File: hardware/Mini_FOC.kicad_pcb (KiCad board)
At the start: 4 copper layers, 63.7 x 41.7 mm, 41 parts, among them J1 Conn_01x03_Socket, J2 Conn_01x06_Socket, J3 Conn_01x04_Socket, J4 Conn_01x04_Socket, J5 Conn_01x02_Socket, J6 Conn_01x06_Socket, SW1 SW_SPDT, U1 DRV8313PWPR, U2 STM32F103C8T6, U3 AMS1117-3.3, U4 LM2596SX-5.0/NOPB, Y2 8MHz

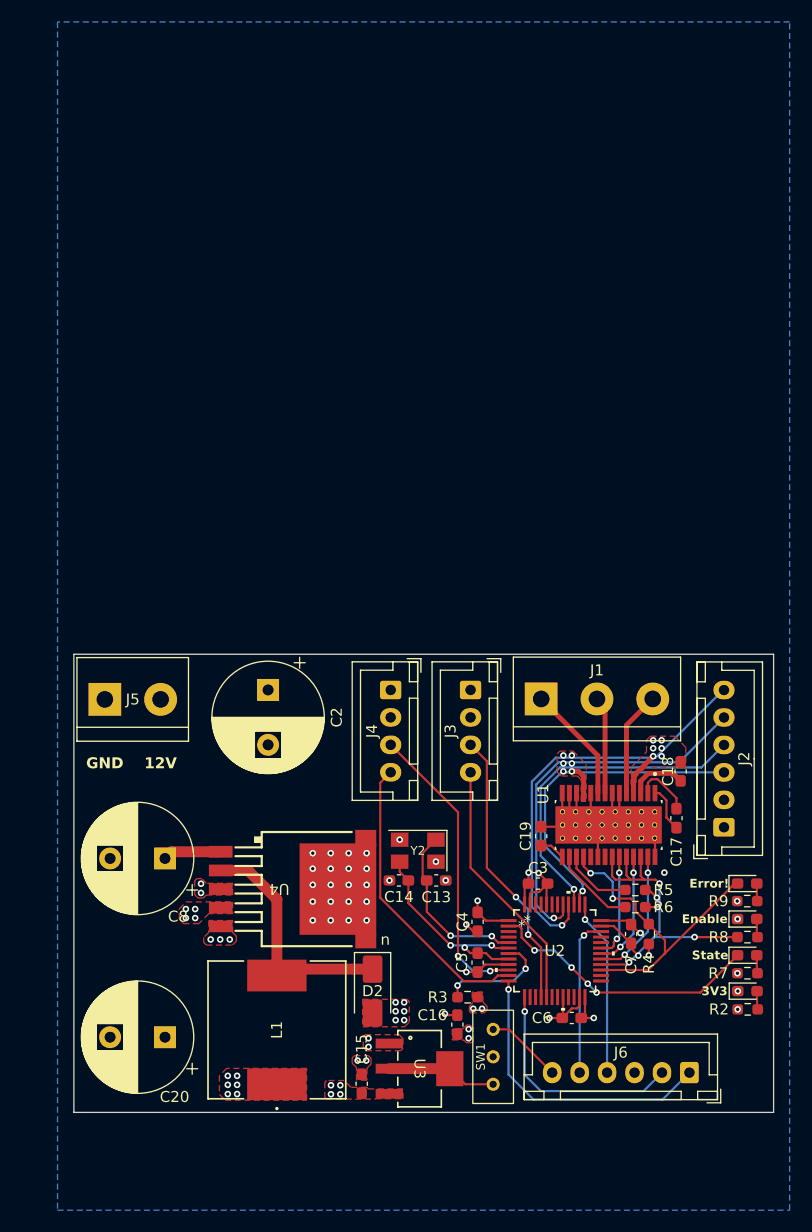
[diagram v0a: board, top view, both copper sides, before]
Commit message: minimize the pcb & add logo
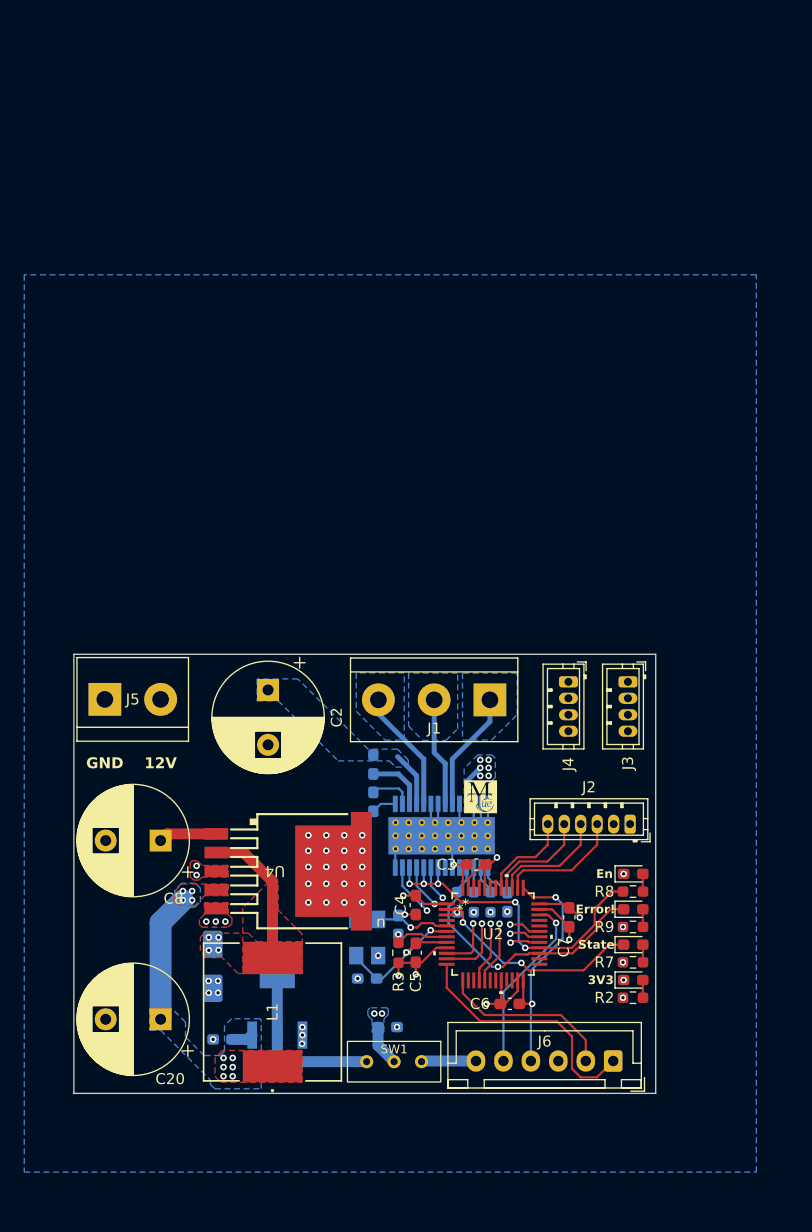
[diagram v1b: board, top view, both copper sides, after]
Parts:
- added G***: LOGO, tue_logo:logo3x3, F.Cu at (85.8, 84.6)
- C13, C14, C15, C16, C17, C18, C19, D2, R4, R5, R6, U1, U3, Y2: moved to B.Cu
- J2: footprint Connector_JST:JST_XH_B6B-XH-A_1x06_P2.50mm_Vertical -> Connector_JST:JST_ZH_B6B-ZR_1x06_P1.50mm_Vertical
- J3, J4: footprint Connector_JST:JST_XH_B4B-XH-A_1x04_P2.50mm_Vertical -> Connector_JST:JST_ZH_B4B-ZR_1x04_P1.50mm_Vertical
- moved C18 28.0 mm to (76.1, 81.7)
- moved C17 27.7 mm to (76.1, 85.1)
- moved R4 17.7 mm to (83.7, 94.2)
- moved J4 16.2 mm to (93.8, 74.1)
- moved U1 15.2 mm to (82.3, 88.2)
- moved R5 14.8 mm to (85.2, 94.2), turned to -90 degrees
- moved D2 14.7 mm to (61.4, 100.0)
- moved J3 14.4 mm to (99.3, 74.1)
- moved U3 14.2 mm to (67.3, 103.6), turned to 180 degrees
- moved C15 13.3 mm to (62.3, 106.7), turned to 180 degrees
- moved R6 13.2 mm to (86.7, 94.2), turned to -90 degrees
- moved R8 11.2 mm to (99.7, 93.2)
- moved D4 11.2 mm to (99.7, 91.6)
- moved R9 10.7 mm to (99.7, 96.5)
- moved D5 10.6 mm to (99.7, 94.8)
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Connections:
- J2 pad 5: SPI_MOSI -> SPI_MISO
- J2 pad 6: SPI_MISO -> SPI_MOSI
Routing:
- net SPI_MISO: track 38.0 -> 9.47 mm, vias 1 -> 0
- net SPI_MOSI: track 34.6 -> 8.51 mm, vias 1 -> 0
- net SPI_CLK: track 30.3 -> 10.4 mm, vias 1 -> 0
- net SPI_SS: track 29.0 -> 11.4 mm, vias 1 -> 0
- net +5V: track 0.08 -> 13.7 mm, vias 14 -> 10
- net Net-(U2A-OSC_IN): track 15.8 -> 7.11 mm, vias 2 -> 1
- net ENC2_CH2: track 23.3 -> 31.8 mm, vias 0 -> 1
- net Net-(D2-K): track 22.1 -> 14.0 mm, vias 0 -> 4
- net ENC2_CH1: track 25.6 -> 32.9 mm, vias 2 -> 1
- net Net-(U2A-NRST): track 10.5 -> 4.82 mm, vias 2 -> 0
- net 3v3_ldo: track 10.0 -> 15.7 mm
- net PWM3: track 9.57 -> 14.9 mm
- net LED_PC13: track 25.3 -> 19.9 mm, vias 4 -> 2
- net PWM2: track 10.7 -> 15.8 mm
- net Net-(U1-~{RESET}): track 7.61 -> 2.60 mm
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- added copper zone on B.Cu, net +12V
- added copper zone on B.Cu, net +3V3
- added copper zone on B.Cu, net +5V
- added copper zone on B.Cu, net MOTOR_PH1
- added copper zone on B.Cu, net MOTOR_PH2
- added copper zone on B.Cu, net MOTOR_PH3
- added copper zone on F.Cu, net Net-(D2-K)
- removed copper zone on F.Cu, net +12V
- removed copper zone on F.Cu, net +3V3
- removed copper zone on In2.Cu, net +5V
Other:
- board size 63.7 x 41.7 mm -> 53 x 40 mm
- board text added: "ENC1"
- board text added: "ENC2"
- board text added: "En"
- board text removed: "3V3-BMP"
- board text removed: "3V3-LDO"
- board text removed: "ECN12"
- board text removed: "ENC11"
- board text removed: "ENC21"
- board text removed: "ENC22"
- board text removed: "Enable"
- board text removed: "SCK"

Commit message: replace power connector
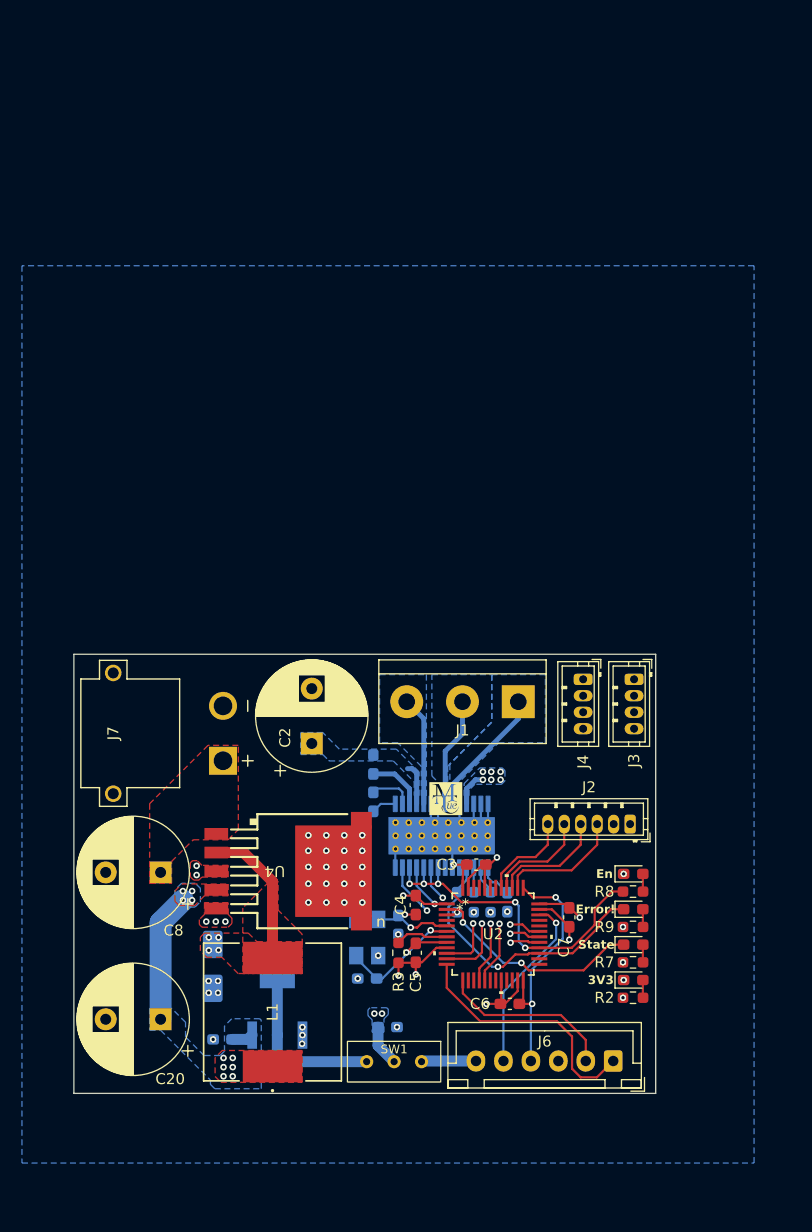
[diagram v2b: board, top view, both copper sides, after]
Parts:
- removed J5: Conn_01x02_Socket, TerminalBlock:TerminalBlock_bornier-2_P5.08mm
- added J7: XT30PW-M, tue_xt30pw-m:AMASS_XT30PW-M, F.Cu at (52.4, 78.8)
- moved C2 6.30 mm to (70.5, 79.7), turned to 90 degrees
- moved G*** 3.17 mm to (82.7, 84.8)
- moved C8 2.90 mm to (56.7, 91.5)
- moved J1 2.59 mm to (89.3, 75.9)
- moved J4 1.36 mm to (95.2, 73.9)
- moved J3 0.61 mm to (99.8, 73.9)
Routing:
- net +12V: track 14.7 -> 7.02 mm
- net ENC2_CH2: track 31.8 -> 29.3 mm
- net ENC2_CH1: track 32.9 -> 31.0 mm
- net MOTOR_PH1: track 11.2 -> 9.95 mm
- net ENC1_CH1: track 28.2 -> 29.2 mm
- net MOTOR_PH3: track 10.9 -> 11.8 mm
- added copper zone on F.Cu, net +12V
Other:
- board text added: "E1"
- board text added: "E2"
- board text added: "G"
- board text added: "V"
- board text removed: "12V"
- board text removed: "ENC1"
- board text removed: "ENC2"
